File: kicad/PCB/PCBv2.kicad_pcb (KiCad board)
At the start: 2 copper layers, 80 x 55 mm, 53 parts, among them J1 JST_2mm, J2 JST_2mm, J3 3.5mm, J5 Ventilador, J6 48V IN, J7 3.5mm, J9 Selector_TC4420, Q1 IRL520N, SW1 SW_DIP_x03, U1 XIAO-RP2350-DIP, U2 AP2112K-3.3, U3 TB6612FNG, U4 TC4420

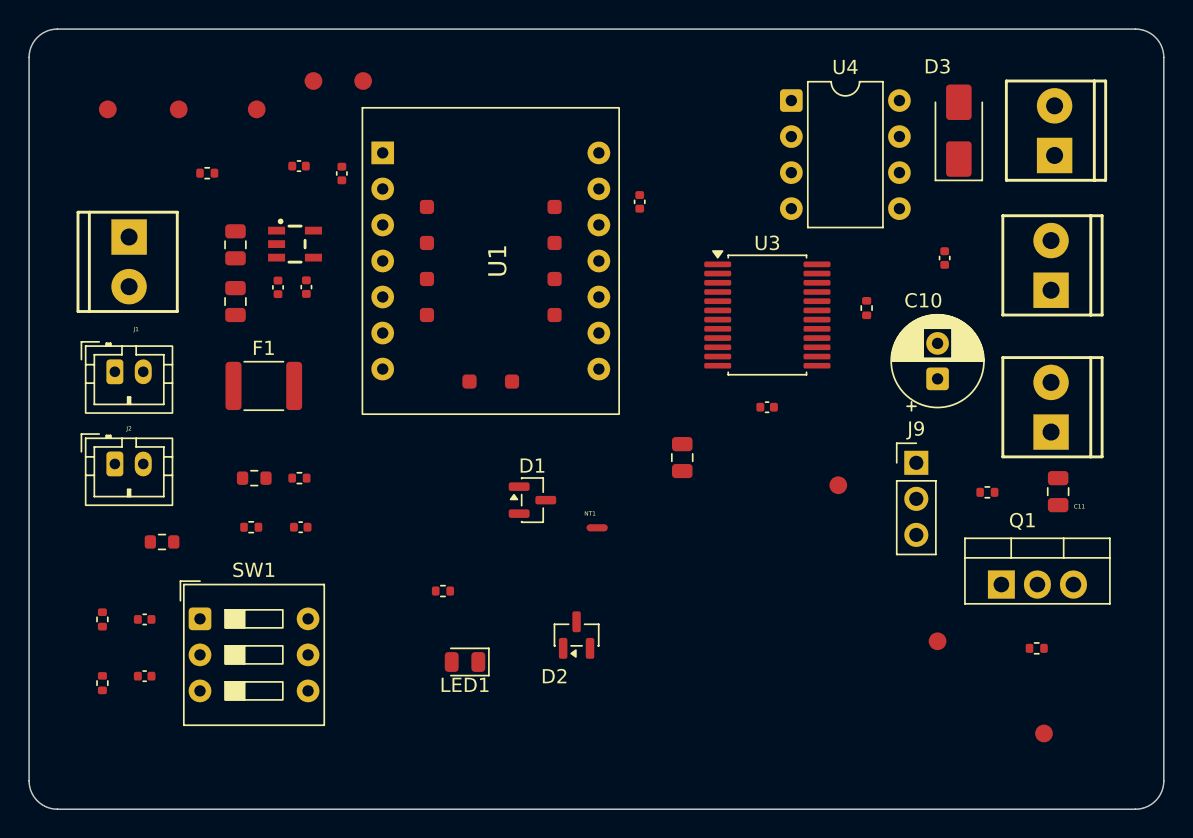
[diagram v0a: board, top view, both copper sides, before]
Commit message: chore: version 1.1.2 - Agregados planos de cobre y organizacion de archivos
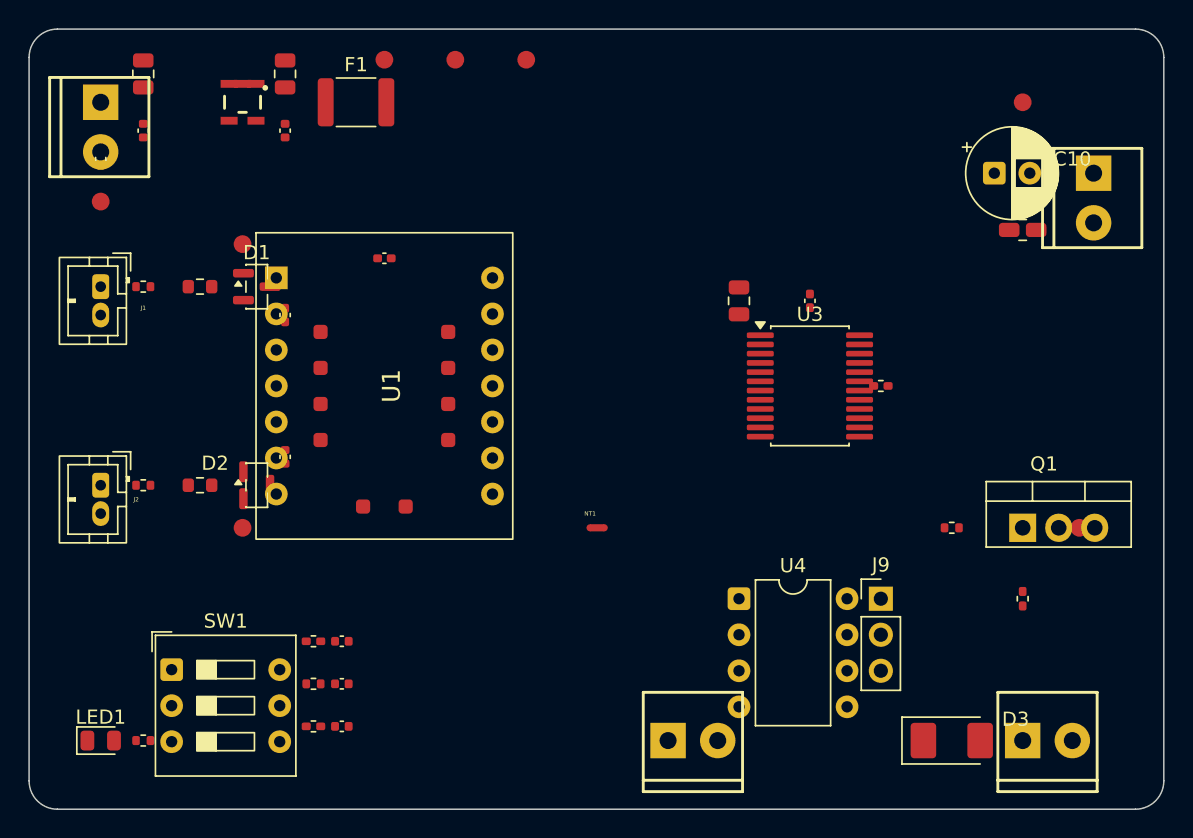
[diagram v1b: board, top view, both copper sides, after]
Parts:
- moved TP4 76.3 mm to (115.0, 82.0)
- moved C15 59.9 mm to (115.0, 79.0), turned to 90 degrees
- moved D3 43.0 mm to (175.0, 120.0), turned to 0 degrees
- moved J3 41.7 mm to (155.0, 120.0), turned to 0 degrees
- moved J5 41.3 mm to (180.0, 120.0), turned to 0 degrees
- moved U4 35.3 mm to (160.0, 110.0)
- moved TP7 32.6 mm to (125.0, 105.0)
- moved TP3 30.0 mm to (180.0, 75.0)
- moved LED1 26.3 mm to (115.0, 120.0), turned to 0 degrees
- moved D2 24.9 mm to (126.0, 102.0), turned to 0 degrees
- moved D1 24.6 mm to (126.0, 88.0)
- moved R_LED1 23.6 mm to (118.0, 120.0)
- moved R4 22.5 mm to (118.0, 102.0)
- moved F1 21.0 mm to (133.0, 75.0)
- moved C6 20.4 mm to (128.0, 100.0)
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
